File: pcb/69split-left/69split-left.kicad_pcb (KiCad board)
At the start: 2 copper layers, 157.5 x 108.9 mm, 94 parts, among them J1 USB_C_Receptacle_USB2.0_16P, J2 Conn_02x03_Odd_Even, J3 USB_C_Receptacle_USB2.0_16P, J4 Conn_01x09_Socket, SW1 SW_Push, SW10 SW_Push, SW11 SW_Push, SW12 SW_Push, SW13 SW_Push, SW14 SW_Push, SW15 SW_Push, SW16 SW_Push, SW17 SW_Push, SW18 SW_Push, SW19 SW_Push, SW2 SW_Push, SW20 SW_Push, SW21 SW_Push, SW22 SW_Push, SW23 SW_Push, SW24 SW_Push, SW25 SW_Push, SW26 SW_Push, SW27 SW_Push, SW28 SW_Push, SW29 SW_Push, SW3 SW_Push, SW30 SW_Push, SW31 SW_Push, SW4 SW_Push, SW5 SW_Push, SW6 SW_Push, SW7 SW_Push, SW8 SW_Push, SW9 SW_Push, U1 ATmega32U4-AU, U2 TLV76133DCY, Y1 Crystal

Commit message: Finished design and layout?
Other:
- board text added: "PB0"
- board text added: "PF0"
- board text added: "PF1"
- board text added: "PF4"
- board text removed: "PB0/CS"
- board text removed: "PF0/ADC0"
- board text removed: "PF1/ADC1"
- board text removed: "PF4/ADC4"
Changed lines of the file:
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@@
 		(allow_soldermask_bridges_in_footprints no)
 		(tenting front back)
+		(grid_origin 59.6 143.14)
 		(pcbplotparams
 			(layerselection 0x00000000_00000000_55555555_5755f5ff)
@@
 		(tags "Cherry MX keyswitch 1.00u PCB")
 		(property "Reference" "SW2"
-			(at -2.54 -2.794 0)
+			(at -2.54 -2.974 0)
 			(layer "F.SilkS")
 			(effects
 				(font
-					(size 1 1)
-					(thickness 0.15)
+					(size 0.7 0.7)
+					(thickness 0.12)
 				)
 			)
@@
 		(tags "Cherry MX keyswitch 1.00u PCB")
 		(property "Reference" "SW3"
-			(at -2.54 -2.794 0)
+			(at -2.54 -2.974 0)
 			(layer "F.SilkS")
 			(effects
 				(font
-					(size 1 1)
-					(thickness 0.15)
+					(size 0.7 0.7)
+					(thickness 0.12)
 				)
 			)
@@
 		(layer "Edge.Cuts")
 	)
-	(gr_text "PB0/CS"
-		(at 99.5775 37.97 90)
+	(gr_text "PB0"
+		(at 99.5775 37.79 90)
 		(layer "F.SilkS" knockout)
 		(effects
 			(font
-				(size 0.5 0.5)
-				(thickness 0.1)
+				(size 0.7 0.7)
+				(thickness 0.12)
 				(bold yes)
 			)
@@
 	)
 	(gr_text "USB5V"
-		(at 81.745 38.08 90)
+		(at 81.745 37.9 90)
 		(layer "F.SilkS" knockout)
 		(effects
 			(font
-				(size 0.5 0.5)
-				(thickness 0.1)
+				(size 0.7 0.7)
+				(thickness 0.12)
 				(bold yes)
 			)
@@
 	)
 	(gr_text "GND"
-		(at 107.21 37.99 90)
+		(at 107.21 37.81 90)
 		(layer "F.SilkS" knockout)
 		(effects
 			(font
-				(size 0.5 0.5)
-				(thickness 0.1)
+				(size 0.7 0.7)
+				(thickness 0.12)
 				(bold yes)
 			)
@@
 		)
 	)
-	(gr_text "PF0/ADC0"
-		(at 91.935 37.97 90)
+	(gr_text "PF0"
+		(at 91.935 37.79 90)
 		(layer "F.SilkS" knockout)
 		(effects
 			(font
-				(size 0.5 0.5)
-				(thickness 0.1)
+				(size 0.7 0.7)
+				(thickness 0.12)
 				(bold yes)
 			)
@@
 		)
 	)
-	(gr_text "PF4/ADC4"
-		(at 97.03 37.97 90)
+	(gr_text "PF4"
+		(at 97.03 37.79 90)
 		(layer "F.SilkS" knockout)
 		(effects
 			(font
-				(size 0.5 0.5)
-				(thickness 0.1)
+				(size 0.7 0.7)
+				(thickness 0.12)
 				(bold yes)
 			)
@@
 	)
 	(gr_text "RX"
-		(at 86.84 38 90)
+		(at 86.84 37.82 90)
 		(layer "F.SilkS" knockout)
 		(effects
 			(font
-				(size 0.5 0.5)
-				(thickness 0.1)
+				(size 0.7 0.7)
+				(thickness 0.12)
 				(bold yes)
 			)
@@
 		)
 	)
-	(gr_text "PF1/ADC1"
-		(at 94.4825 37.97 90)
+	(gr_text "PF1"
+		(at 94.4825 37.79 90)
 		(layer "F.SilkS" knockout)
 		(effects
 			(font
-				(size 0.5 0.5)
-				(thickness 0.1)
+				(size 0.7 0.7)
+				(thickness 0.12)
 				(bold yes)
 			)
@@
 	)
 	(gr_text "SDA"
-		(at 102.08 38.03 90)
+		(at 102.08 37.85 90)
 		(layer "F.SilkS" knockout)
 		(effects
 			(font
-				(size 0.5 0.5)
-				(thickness 0.1)
+				(size 0.7 0.7)
+				(thickness 0.12)
 				(bold yes)
 			)
@@
 	)
 	(gr_text "2RIGHT"
-		(at 206.04 38.07 0)
+		(at 206.04 38.18 0)
 		(layer "F.SilkS" knockout)
 		(effects
@@
 	)
 	(gr_text "3V3"
-		(at 84.29 37.98 90)
+		(at 84.29 37.8 90)
 		(layer "F.SilkS" knockout)
 		(effects
 			(font
-				(size 0.5 0.5)
-				(thickness 0.1)
+				(size 0.7 0.7)
+				(thickness 0.12)
 				(bold yes)
 			)
@@
 	)
 	(gr_text "TX"
-		(at 89.3875 38 90)
+		(at 89.3875 37.82 90)
 		(layer "F.SilkS" knockout)
 		(effects
 			(font
-				(size 0.5 0.5)
-				(thickness 0.1)
+				(size 0.7 0.7)
+				(thickness 0.12)
 				(bold yes)
 			)
@@
 	)
 	(gr_text "SCL"
-		(at 104.58 38.03 90)
+		(at 104.58 37.85 90)
 		(layer "F.SilkS" knockout)
 		(effects
 			(font
-				(size 0.5 0.5)
-				(thickness 0.1)
+				(size 0.7 0.7)
+				(thickness 0.12)
 				(bold yes)
 			)

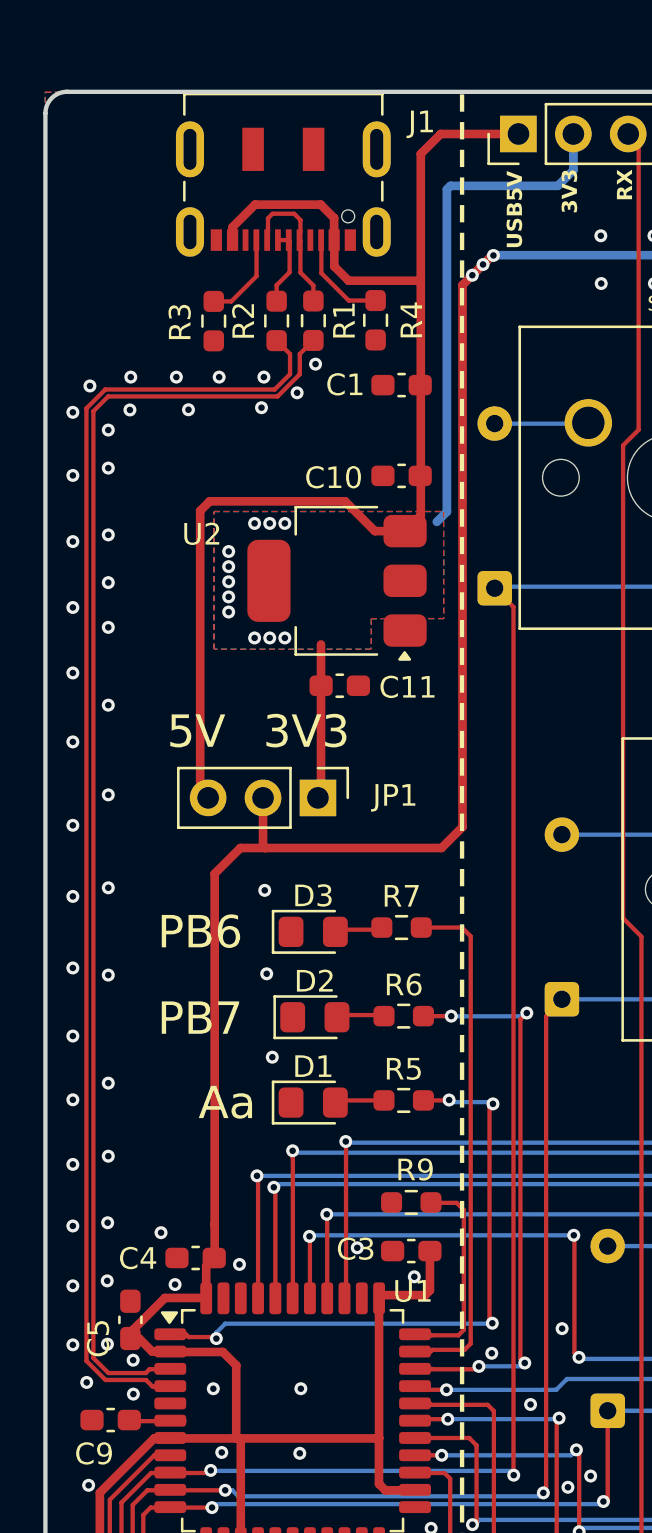
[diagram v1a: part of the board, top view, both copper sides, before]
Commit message: Added ESD protection and better routing for the USB data lines.
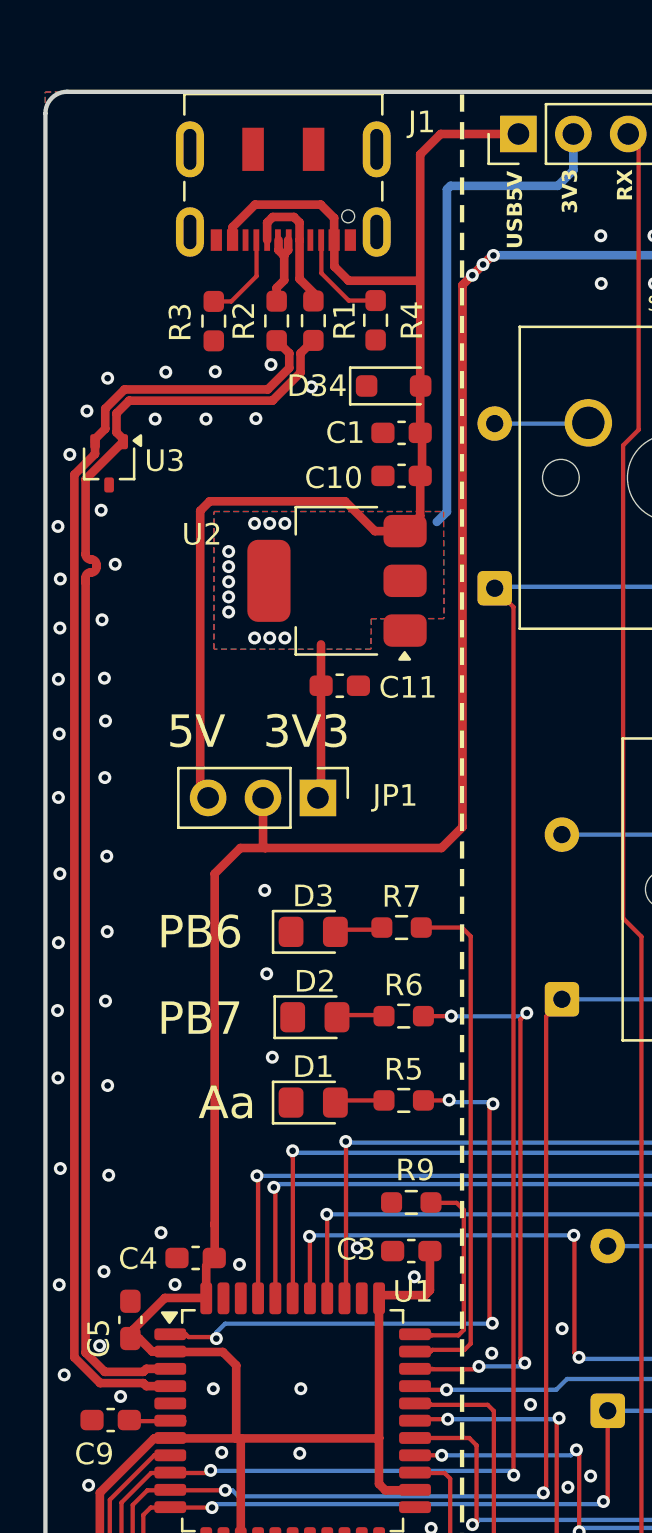
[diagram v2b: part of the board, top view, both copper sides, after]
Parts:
- added D34: DESD5V0S1BA, Diode_SMD:D_SOD-323_HandSoldering, F.Cu at (75.7, 47.9)
- added U3: TPD2E2U06DCK, Package_TO_SOT_SMD:SOT-323_SC-70, F.Cu at (62.6, 51.4)
- moved C1 2.21 mm to (76.1, 50.0)
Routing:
- net GND: vias 98 -> 93

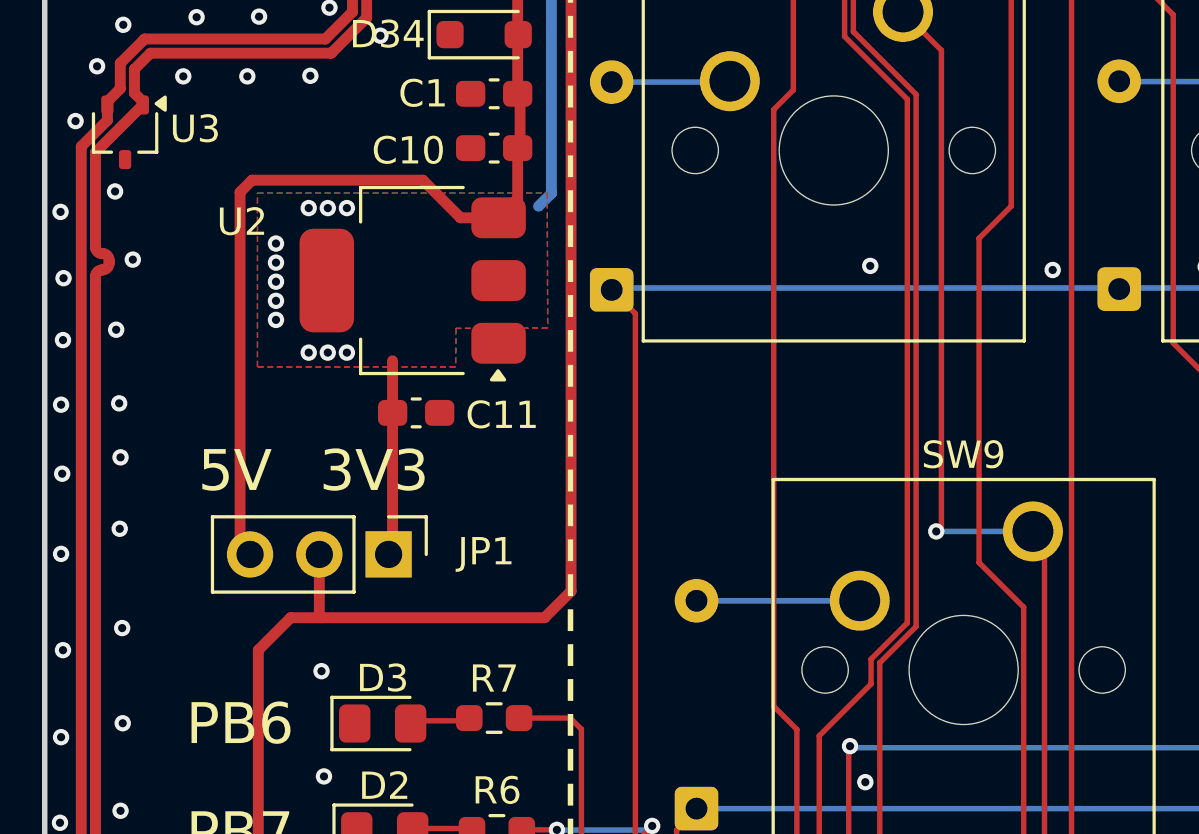
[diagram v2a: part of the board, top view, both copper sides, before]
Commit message: Added SPDT switch because I do not want to wait for the KiCAD librarians to approve of my SP3T switch, therefore that will be in future work.
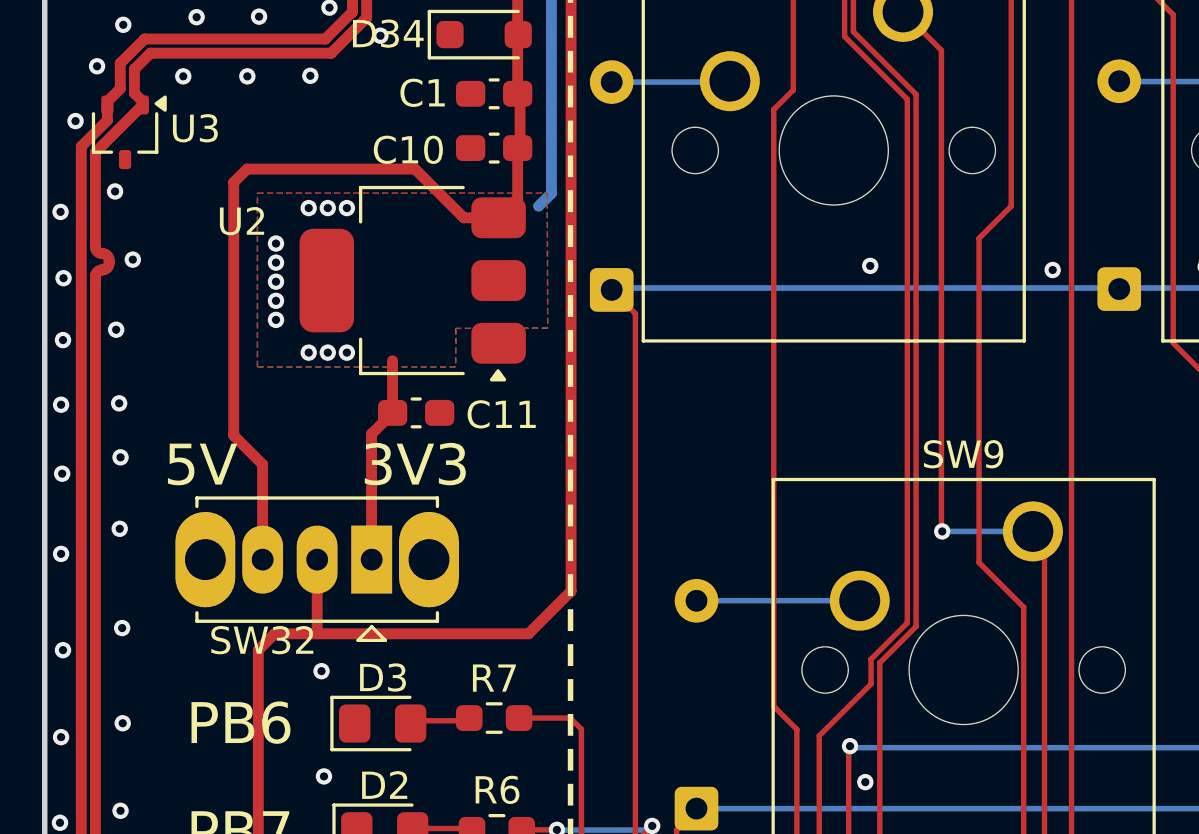
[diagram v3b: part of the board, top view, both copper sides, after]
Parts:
- removed JP1: Jumper_3_Bridged12, Connector_PinHeader_2.54mm:PinHeader_1x03_P2.54mm_Vertical
- added SW32: SW_SPDT, Button_Switch_THT:SW_Slide_SPDT_Straight_CK_OS102011MS2Q, F.Cu at (71.6, 67.1)
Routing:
- net /USB_5V: track 58.8 -> 61.0 mm

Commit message: Final touches.
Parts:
- C6: value 1u -> 100n
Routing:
- net /ATmega32U4/COL6: track 204.8 -> 206.4 mm
- net /ATmega32U4/COL4: track 199.2 -> 200.5 mm
- net /ATmega32U4/GPIO_OUT_PB6: track 174.1 -> 175.0 mm

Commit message: Ordered the PCBs and parts!
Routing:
- net /ATmega32U4/GPIO_OUT_PB6: track 175.0 -> 173.9 mm
- net /ATmega32U4/ADC4: track 80.5 -> 81.3 mm
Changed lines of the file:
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@@
 	)
 	(gr_line
-		(start 60.61 34.237091)
-		(end 211.36 34.237091)
+		(start 60.61 34.24)
+		(end 211.36 34.24)
 		(stroke
 			(width 0.2)
@@
 	)
 	(gr_arc
-		(start 59.61 35.237091)
-		(mid 59.902896 34.53)
-		(end 60.61 34.237091)
+		(start 59.6129 35.237091)
+		(mid 59.904947 34.532041)
+		(end 60.61 34.24)
 		(stroke
 			(width 0.2)
@@
 	)
 	(gr_line
-		(start 212.36 35.24)
+		(start 212.36 35.239623)
 		(end 212.369579 60.629579)
 		(stroke
@@
 		(layer "Dwgs.User")
 		(pts
-			(xy 60 143.14) (xy 59.902896 34.25)
+			(xy 59.81 143.140085) (xy 60.49 34.24)
 		)
-		(height -3.71)
+		(height -3.7)
 		(orientation 1)
 		(format
@@
 			(keep_text_aligned yes)
 		)
-		(gr_text "108.89 mm"
-			(at 55.14 88.695 90)
+		(gr_text "108.90 mm"
+			(at 54.96 88.690042 90)
 			(layer "Dwgs.User")
 			(effects
@@
 	)
 	(segment
+		(start 97.260715 83.370715)
+		(end 97.260715 68.639285)
+		(width 0.2)
+		(layer "F.Cu")
+		(net 54)
+	)
+	(segment
+		(start 97.260715 68.639285)
+		(end 98.21 67.69)
+		(width 0.2)
+		(layer "F.Cu")
+		(net 54)
+	)
+	(segment
+		(start 97.26 43.42)
+		(end 96.74 42.9)
+		(width 0.2)
+		(layer "F.Cu")
+		(net 54)
+	)
+	(segment
 		(start 71.06 83.539)
 		(end 71.06 90.0575)
@@
 	)
 	(segment
-		(start 96.74 42.9)
-		(end 96.74 36.19)
+		(start 98.21 63.93)
+		(end 97.26 62.98)
 		(width 0.2)
 		(layer "F.Cu")
@@
 	)
 	(segment
-		(start 97.260715 43.420715)
-		(end 96.74 42.9)
+		(start 98.21 67.69)
+		(end 98.21 63.93)
+		(width 0.2)
+		(layer "F.Cu")
+		(net 54)
+	)
+	(segment
+		(start 96.74 42.9)
+		(end 96.74 36.19)
 		(width 0.2)
 		(layer "F.Cu")
@@
 	)
 	(segment
-		(start 97.260715 83.370715)
-		(end 97.260715 43.420715)
+		(start 97.26 62.98)
+		(end 97.26 43.42)
 		(width 0.2)
 		(layer "F.Cu")
@@
 	)
 	(segment
-		(start 190.26 70.39)
-		(end 191.31 69.34)
+		(start 76.8825 94.3)
+		(end 76.7125 94.13)
 		(width 0.2)
 		(layer "F.Cu")
@@
 	)
 	(segment
-		(start 191.65 43.96028)
-		(end 191.65 41.1)
+		(start 191.61 39.97)
+		(end 191.65 40.01)
 		(width 0.2)
 		(layer "F.Cu")
@@
 	)
 	(segment
-		(start 76.8825 94.3)
-		(end 76.7125 94.13)
+		(start 190.26 72.03)
+		(end 190.26 70.39)
 		(width 0.2)
 		(layer "F.Cu")
@@
 	)
 	(segment
-		(start 191.61 39.97)
-		(end 191.65 40.01)
+		(start 191.65 40.01)
+		(end 191.65 41.1)
 		(width 0.2)
 		(layer "F.Cu")
@@
 	)
 	(segment
-		(start 191.31 69.34)
-		(end 191.31 64.79)
+		(start 191.54 39.97)
+		(end 191.61 39.97)
 		(width 0.2)
 		(layer "F.Cu")
@@
 	)
 	(segment
-		(start 191.65 40.01)
+		(start 191.65 43.96028)
 		(end 191.65 41.1)
 		(width 0.2)
@@
 	)
 	(segment
-		(start 191.78 73.55)
-		(end 190.26 72.03)
+		(start 194.51 39.99)
+		(end 194.65 40.13)
 		(width 0.2)
 		(layer "F.Cu")
@@
 	)
 	(segment
-		(start 190.88 64.36)
-		(end 190.88 44.73028)
+		(start 191.31 64.79)
+		(end 190.88 64.36)
 		(width 0.2)
 		(layer "F.Cu")
@@
 	)
 	(segment
-		(start 191.54 39.97)
-		(end 191.61 39.97)
+		(start 191.31 69.34)
+		(end 191.31 64.79)
 		(width 0.2)
 		(layer "F.Cu")
@@
 	)
 	(segment
-		(start 194.51 39.99)
-		(end 194.65 40.13)
+		(start 191.07 72.84)
+		(end 190.26 72.03)
 		(width 0.2)
 		(layer "F.Cu")
@@
 	)
 	(segment
-		(start 190.26 72.03)
-		(end 190.26 70.39)
+		(start 190.88 64.36)
+		(end 190.88 44.73028)
 		(width 0.2)
 		(layer "F.Cu")
@@
 	)
 	(segment
-		(start 191.31 64.79)
-		(end 190.88 64.36)
+		(start 194.65 40.13)
+		(end 194.65 41.1)
 		(width 0.2)
 		(layer "F.Cu")
@@
 	)
 	(segment
-		(start 190.88 44.73028)
-		(end 191.65 43.96028)
+		(start 191.07 93.68)
+		(end 191.07 72.84)
 		(width 0.2)
 		(layer "F.Cu")
@@
 	)
 	(segment
-		(start 194.65 40.13)
-		(end 194.65 41.1)
+		(start 190.26 70.39)
+		(end 191.31 69.34)
 		(width 0.2)
 		(layer "F.Cu")
@@
 	)
 	(segment
-		(start 191.78 93.82)
-		(end 191.78 73.55)
+		(start 190.88 44.73028)
+		(end 191.65 43.96028)
 		(width 0.2)
 		(layer "F.Cu")
@@
 	)
 	(via
-		(at 191.78 93.82)
+		(at 191.07 93.68)
 		(size 0.6)
 		(drill 0.3)
@@
 	(segment
 		(start 83.246 94.3)
-		(end 83.746 93.8)
+		(end 78.17 94.3)
 		(width 0.2)
 		(layer "B.Cu")
@@
 	)
 	(segment
-		(start 83.746 93.8)
-		(end 191.76 93.8)
+		(start 191.07 93.68)
+		(end 190.95 93.8)
 		(width 0.2)
 		(layer "B.Cu")
@@
 	)
 	(segment
-		(start 78.17 94.3)
+		(start 83.746 93.8)
 		(end 83.246 94.3)
 		(width 0.2)
@@
 	)
 	(segment
-		(start 191.76 93.8)
-		(end 191.78 93.82)
+		(start 190.95 93.8)
+		(end 83.746 93.8)
 		(width 0.2)
 		(layer "B.Cu")
@@
 	)
 	(segment
+		(start 176.99 66.24925)
+		(end 176.80775 66.067)
+		(width 0.2)
+		(layer "F.Cu")
+		(net 62)
+	)
+	(segment
 		(start 167.49 66.13)
 		(end 167.49 47.22425)
@@
 	)
 	(segment
-		(start 176.80775 85.117)
-		(end 176.80775 66.067)
-		(width 0.2)
-		(layer "F.Cu")
-		(net 62)
-	)
-	(segment
 		(start 84.119 87.15)
 		(end 84.09 87.179)
@@
 	)
 	(segment
+		(start 176.99 85.117)
+		(end 176.99 66.24925)
+		(width 0.2)
+		(layer "F.Cu")
+		(net 62)
+	)
+	(segment
 		(start 182.03 92.88)
 		(end 182.01 92.88)
@@
 	)
 	(via
-		(at 176.80775 85.117)
+		(at 176.99 85.117)
 		(size 0.6)
 		(drill 0.3)
@@
 	)
 	(segment
-		(start 181.57025 85.117)
-		(end 176.80775 85.117)
+		(start 182.08 104.17)
+		(end 182.077 104.167)
 		(width 0.2)
 		(layer "B.Cu")
@@
 	)
 	(segment
-		(start 182.08 104.17)
-		(end 182.077 104.167)
+		(start 181.57025 85.117)
+		(end 176.99 85.117)
 		(width 0.2)
 		(layer "B.Cu")
